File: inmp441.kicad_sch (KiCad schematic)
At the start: 9 parts

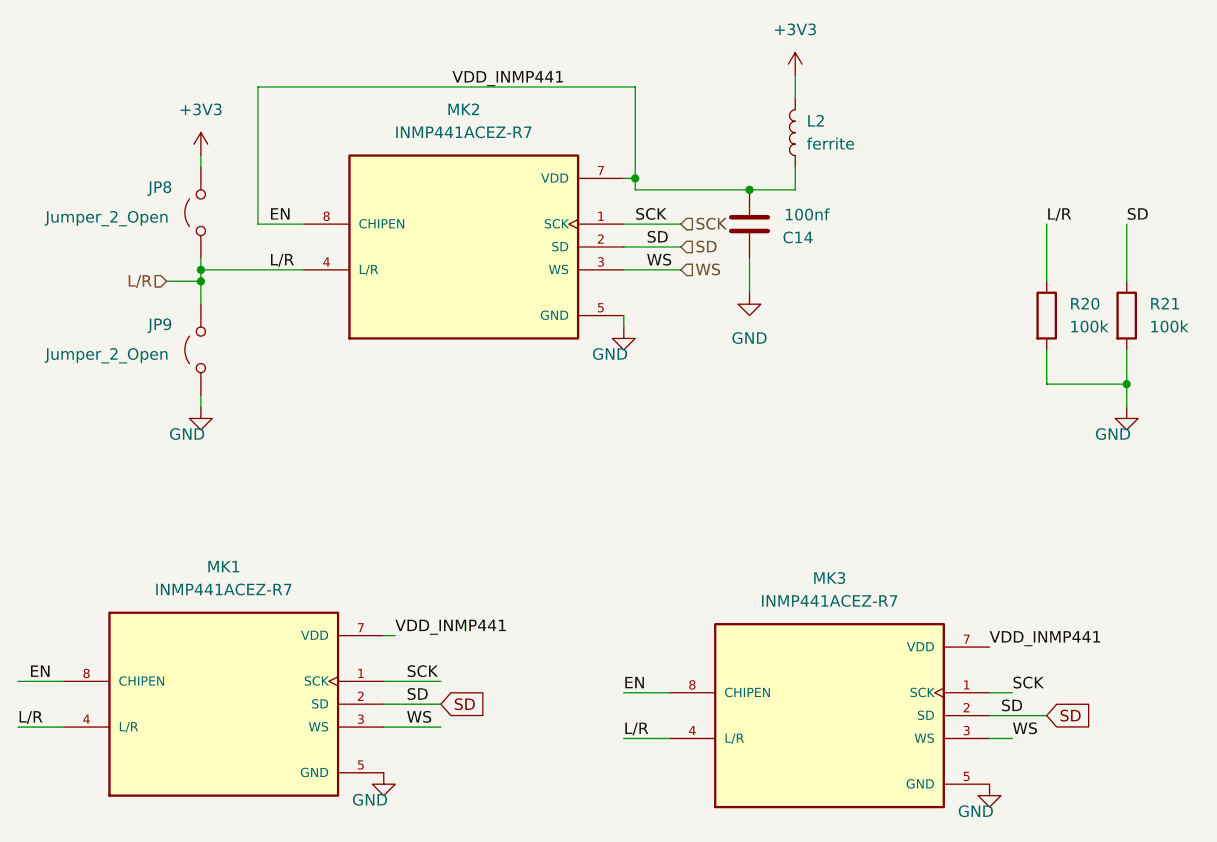
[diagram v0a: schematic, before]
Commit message: se agrego osciloscoio
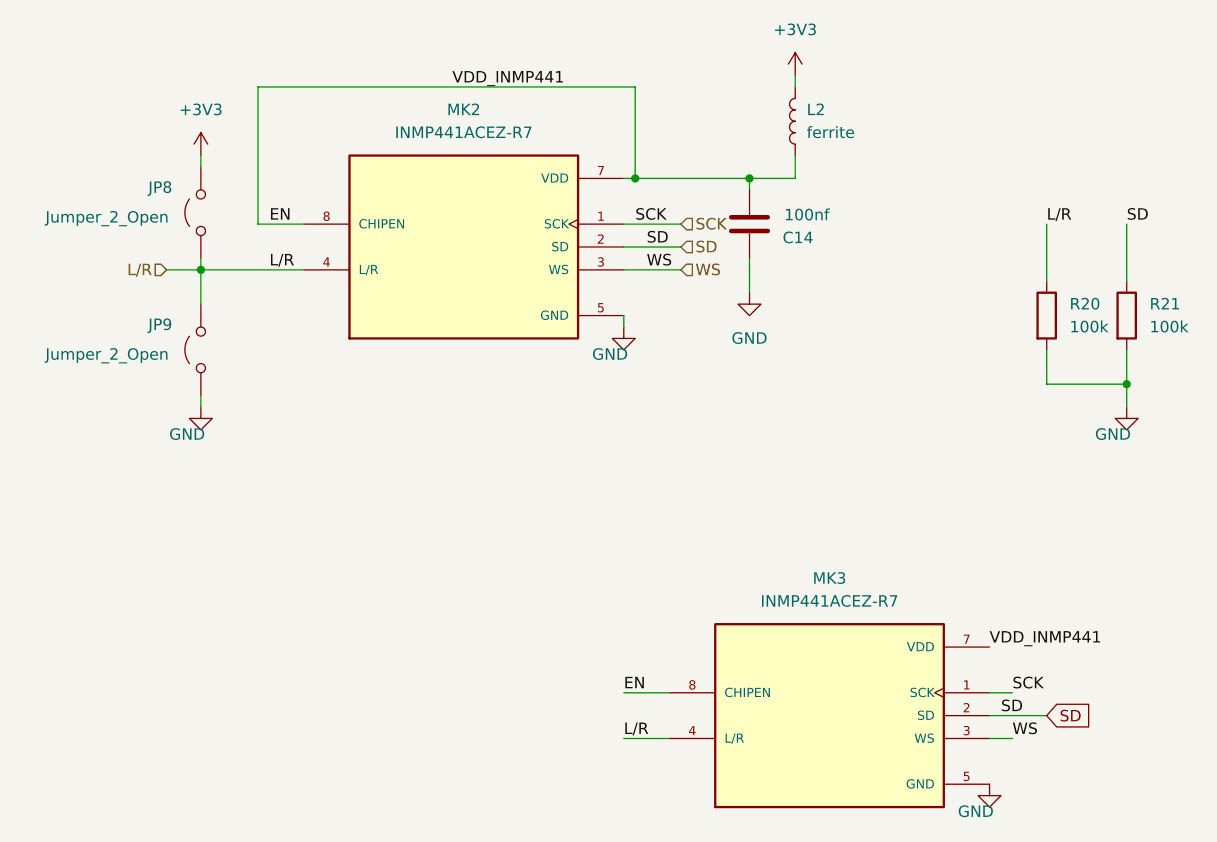
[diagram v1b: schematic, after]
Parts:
- removed MK1: INMP441ACEZ-R7, kiC:MIC_INMP441ACEZ-R7, symbol INMP441ACEZ-R7:INMP441ACEZ-R7
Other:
- moved on the sheet: L2
